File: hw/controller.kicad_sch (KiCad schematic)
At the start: 16 parts, among them J1 BNC, J201 1935776, SW201 SW_Push, U201 MCU_Nucleo_L432KC

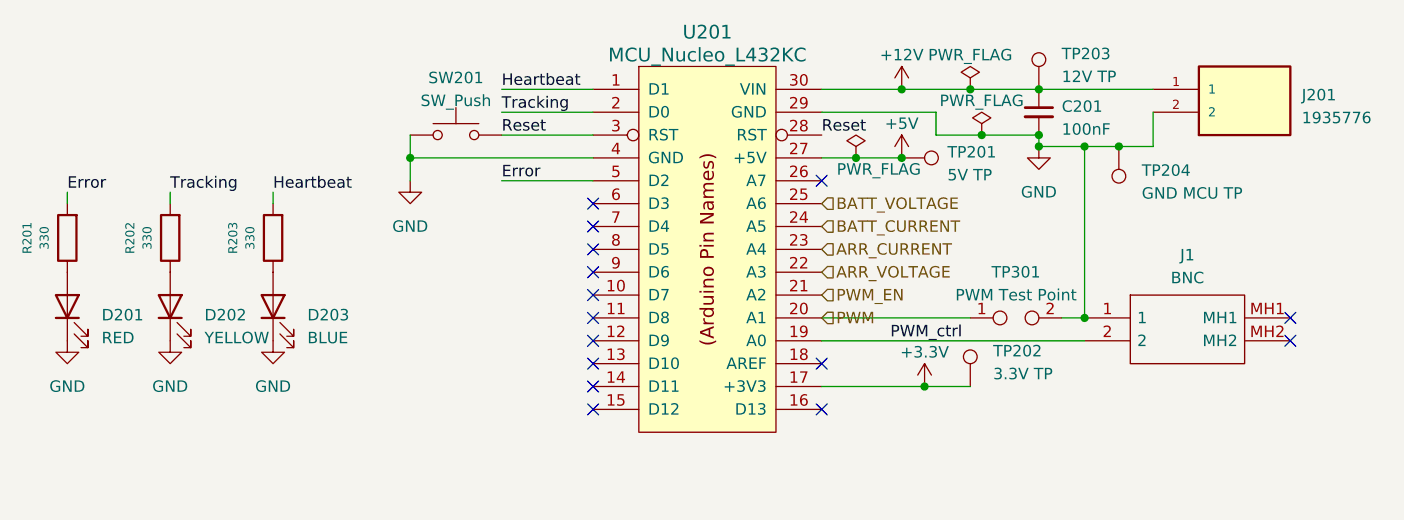
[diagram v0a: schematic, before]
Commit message: rebuild schematic, passes ERC, bom completed
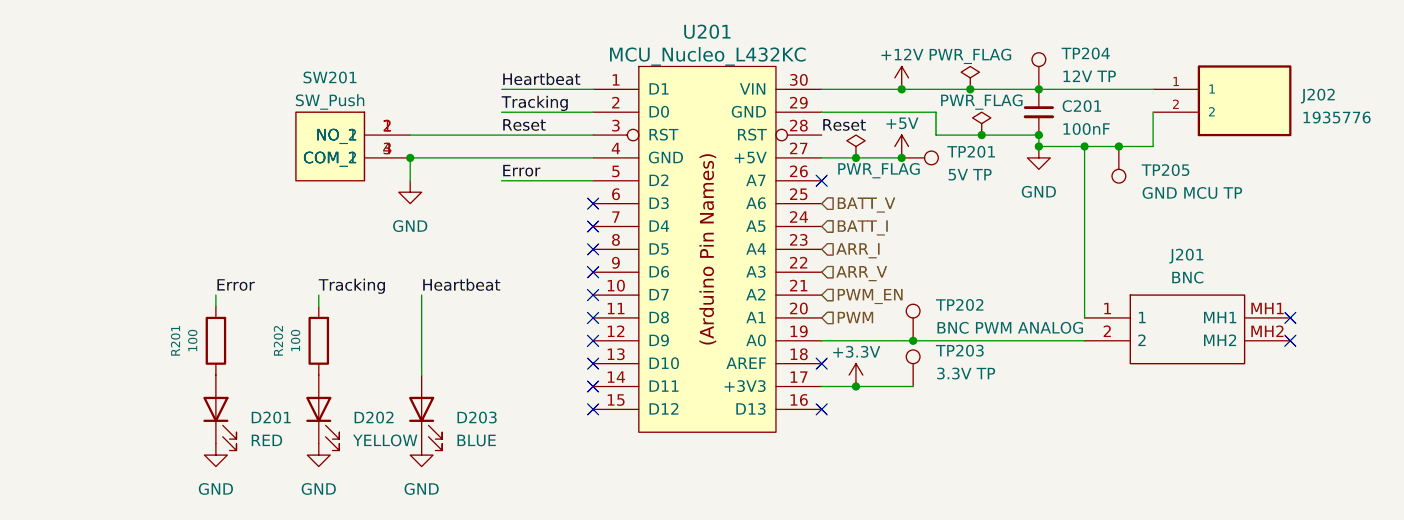
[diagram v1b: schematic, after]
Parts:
- removed R203: 330, Resistor_SMD:R_0805_2012Metric, symbol Device:R
- removed TP301: PWM Test Point, mppt:SignalTP, symbol Connector:TestPoint_2Pole
- added TP202: BNC PWM ANALOG, TestPoint:TestPoint_Keystone_5000-5004_Miniature, symbol Connector:TestPoint
- C201: Distributor (none) -> JLCPCB; In Stock? Y -> (none); JLC P/N (none) -> C307331; Manufacturer (none) -> Samsung Electro-Mechanics; Mfr PN CL21B104KCFNNNE -> (none); P/N (none) -> CL05B104KB54PNC; Projected Cost 0.008 -> (none)
- D201: footprint LED_SMD:LED_0805_2012Metric -> LED_SMD:LED_0402_1005Metric; Distributor (none) -> Mouser; In stock? Y -> (none); Manufacturer (none) -> Kingbright; Mfr PN NCD0805R1 -> (none); P/N (none) -> 604-APHHS1005SURCK; Projected Cost 0.0114 -> (none)
- D202: footprint LED_SMD:LED_0805_2012Metric -> LED_SMD:LED_0402_1005Metric; Distributor (none) -> Mouser; In Stock? Y -> (none); Manufacturer (none) -> Kingbright; Mfr PN SZYY0805YG -> (none); P/N (none) -> 604-APHHS1005SYCK; Projected Cost 0.0123 -> (none)
- D203: footprint LED_SMD:LED_0805_2012Metric -> LED_SMD:LED_0402_1005Metric; Distributor (none) -> Mouser; In Stock? Y -> (none); Manufacturer (none) -> Kingbright; Mfr PN SZYY0805B -> (none); P/N (none) -> 604-APHHS1005QBCD; Projected Cost 0.0129 -> (none)
- J201: renamed from J1; Distributor (none) -> Digikey; Manufacturer (none) -> Adam Tech; Manufacturer_Part_Number RF1-01A-D-00-75-M -> (none); P/N (none) -> 2057-RF1-01A-D-00-75-M-ND
- J202: renamed from J201; footprint 1935776 -> mppt:1935776; DESCRIPTION Fixed Terminal Blocks PT 2.5/ 2-5.0-H g -> (none); Distributor (none) -> Mouser; HEIGHT 13.5mm -> (none); In Stock? Y -> (none); MANUFACTURER_NAME Phoenix Contact -> (none); MANUFACTURER_PART_NUMBER 1935776 -> (none); MOUSER_PART_NUMBER 651-1935776 -> (none); MOUSER_PRICE-STOCK https://www.mouser.co.uk/ProductDetail/Phoenix-Contact/1935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 -> (none); Manufacturer (none) -> Phoenix Contact; P/N (none) -> 651-1935776; Projected Cost 0.59 -> (none)
- R201, R202: value 330 -> 100; footprint Resistor_SMD:R_0805_2012Metric -> Resistor_SMD:R_0402_1005Metric; In Stock? Y -> (none); JLC P/N (none) -> C25076; JLCPCB BOM 1 -> (none); LCSC Part C17630 -> (none); Manufacturer Part Number 0805W8F3300T5E -> (none); Mouser Part N/A -> (none); P/N (none) -> 0402WGF1000TCE; Projected Cost 0.0024 -> (none); Purchase Page N/A -> (none)
- SW201: footprint Button_Switch_THT:SW_PUSH_6mm -> mppt:TS046643BK100SMT; symbol Switch:SW_Push -> TS04-66-43-BK-100-SMT:TS04-66-43-BK-100-SMT; Distributor (none) -> Mouser; Manufacturer (none) -> CUI Devices; P/N (none) -> 179-TS046643BK100SMT
- TP201: Color (none) -> Red; Distributor (none) -> Mouser; Manufacturer (none) -> Keystone Electronics; P/N (none) -> 534-5000
- TP203: renamed from TP202; Color (none) -> Red; Distributor (none) -> Mouser; Manufacturer (none) -> Keystone Electronics; P/N (none) -> 534-5000
- TP204: renamed from TP203; Color (none) -> Red; Distributor (none) -> Mouser; Manufacturer (none) -> Keystone Electronics; P/N (none) -> 534-5000
- TP205: renamed from TP204; Color (none) -> Black; Distributor (none) -> Mouser; Manufacturer (none) -> Keystone Electronics; P/N (none) -> 534-5001
- U201: Distributor (none) -> Mouser; In Stock? N/A -> (none); Manufacturer (none) -> STMicroelectronics; P/N (none) -> 511-NUCLEO-L432KC
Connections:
- net GND: now also SW201.3 (COM_1), SW201.4 (COM_2); no longer SW201.1
- net Heartbeat: now also D203.2 (A)
- net Reset: now also SW201.1 (NO_1)
- net ARR_CURRENT renamed ARR_I
- net ARR_VOLTAGE renamed ARR_V
- net BATT_CURRENT renamed BATT_I
- net BATT_VOLTAGE renamed BATT_V
- net PWM_ctrl: no longer names the net of J201.2, U201.19 (A0)
- net PWM_ctrl: now also TP202.1
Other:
- moved on the sheet: D201, D202, D203, R201, R202, TP203

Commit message: savestate layout
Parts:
- removed J201: BNC, mppt:CONBNC002, symbol CONBNC002:CONBNC002
- removed TP202: BNC PWM ANALOG, TestPoint:TestPoint_Keystone_5000-5004_Miniature, symbol Connector:TestPoint
- added J202: BNC, mppt:CONBNC002, symbol CONBNC002:CONBNC002
- added TP204: TestPoint_2Pole, mppt:SignalTP, symbol Connector:TestPoint_2Pole
- renumbered J202 to J201, TP203 to TP202, TP204 to TP203
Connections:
- net GND: now also J202.2, J202.MH1, J202.MH2, TP204.2
- net at U201.19 (A0): now also J202.1, TP204.1
- no-connect marks 15 -> 13

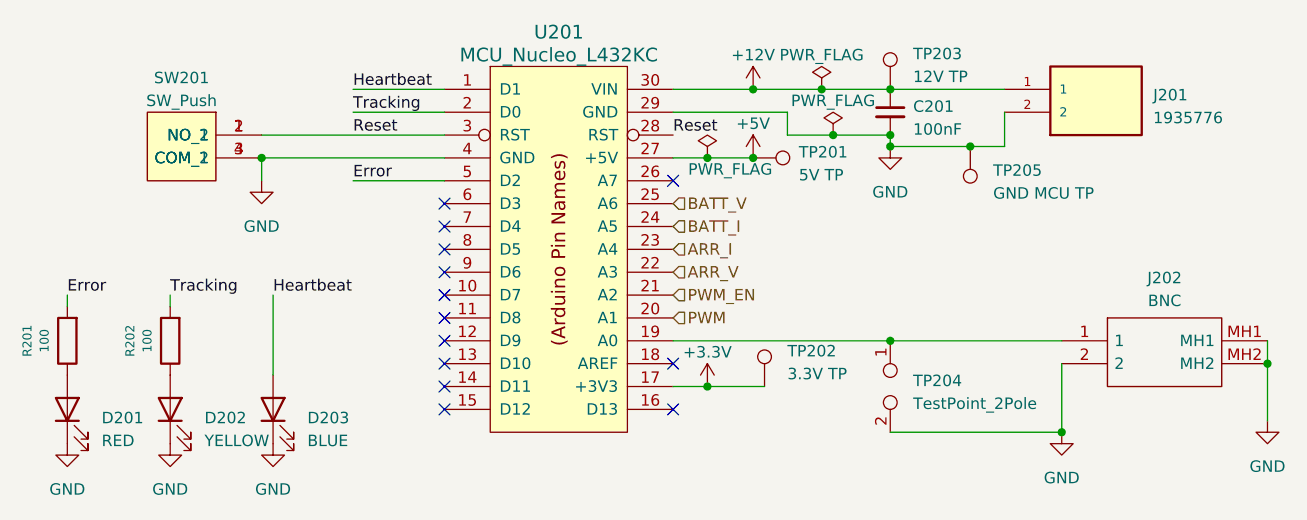
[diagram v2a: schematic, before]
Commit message: production files for v0.1.0. Change cap power calc to be based off i_rms of i_pkpk, not i_pk + r_l_a
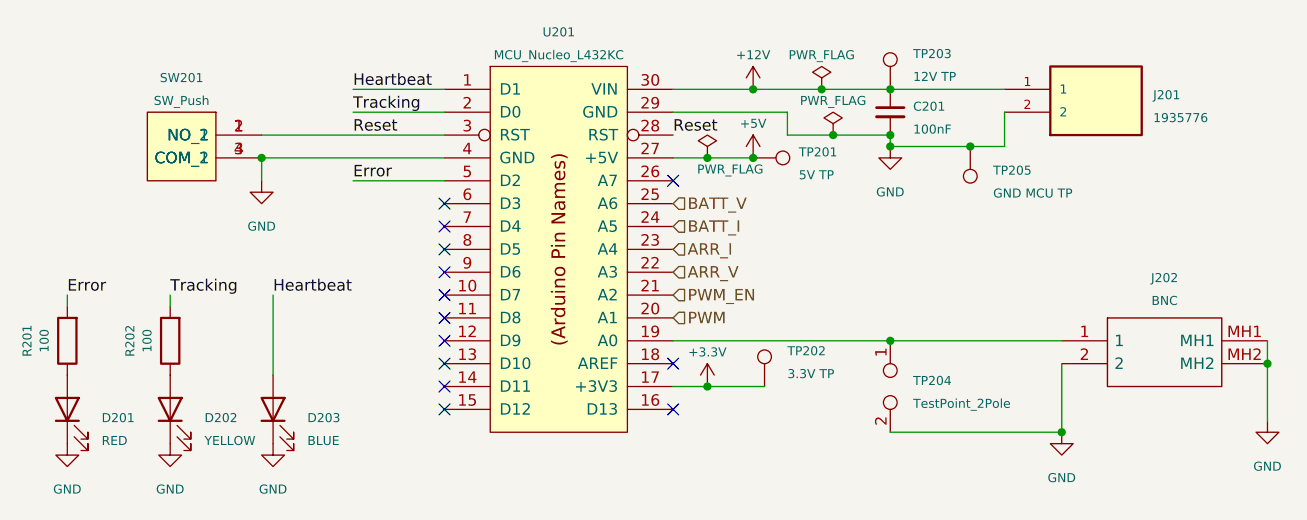
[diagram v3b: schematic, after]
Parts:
- C201: LCSC Part # (none) -> C307331
- R201, R202: LCSC Part # (none) -> C25076

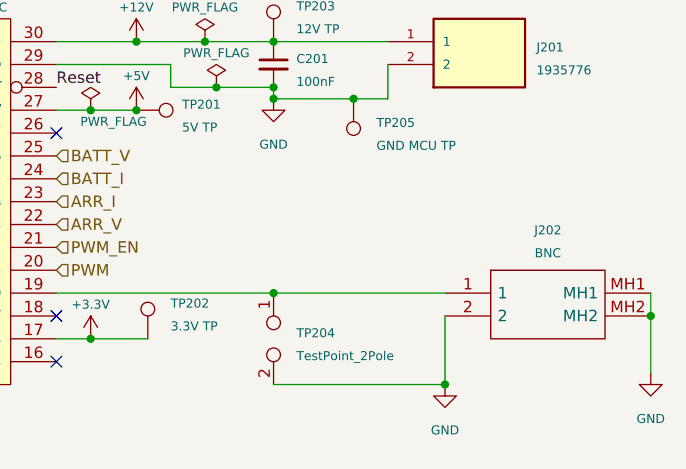
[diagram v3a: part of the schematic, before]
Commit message: fixed gate driver circuit, filleted filled zones, ensured DRC conformity regarding clearances
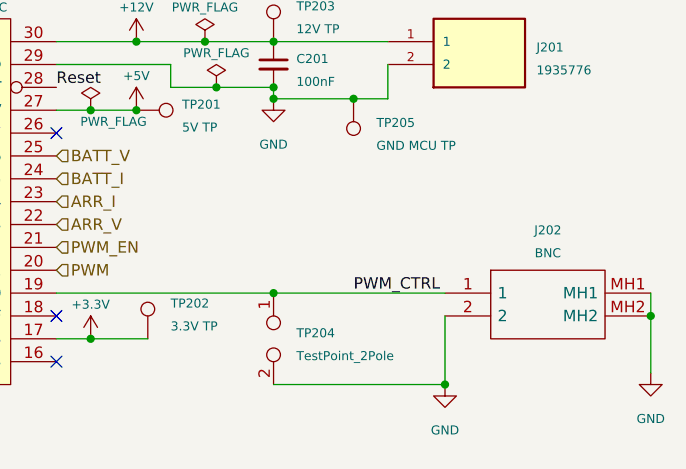
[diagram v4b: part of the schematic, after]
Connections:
- net PWM_CTRL: now reaches J202.1, TP204.1, U201.19 (A0)
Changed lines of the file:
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@@
+    (effects (font (size 1.27 1.27)) (justify left bottom))
+  )
+  (label "PWM_CTRL" (at 199.39 100.33 0) (fields_autoplaced)
     (effects (font (size 1.27 1.27)) (justify left bottom))
   )

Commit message: fixes for v0.1.1rc
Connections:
- net Error: now also U201.6 (D3); no longer U201.5 (D2)
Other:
- note added: "I2C1_SCL"
- note added: "I2C1_SDA"
- note added: "USB_DM|CAN1_RD"
- note added: "USB_DP|CAN1_TD"
- company: (none) -> UT LHR Solar
- title: MPPT -> Sunscatter MPPT
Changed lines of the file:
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@@
   (paper "A4")
   (title_block
-    (title "MPPT")
-    (date "2023-01-30")
-    (rev "v0.0.0")
-    (comment 1 "Nishant Gupta")
+    (title "Sunscatter MPPT")
+    (date "2023-03-26")
+    (rev "v0.1.1")
+    (company "UT LHR Solar")
+    (comment 1 "Matthew Yu")
     (comment 2 "Jacob Pustilnik")
   )
@@
   (no_connect (at 166.37 82.55))
   (no_connect (at 140.97 107.95))
-  (no_connect (at 140.97 85.09))
   (no_connect (at 140.97 87.63))
+  (no_connect (at 140.97 82.55))
   (no_connect (at 166.37 102.87))
   (wire (pts (xy 110.49 95.25) (xy 110.49 96.52))
@@
   )
   (wire (pts (xy 166.37 100.33) (xy 190.5 100.33))
+    (stroke (width 0) (type default))
+  )
+  (wire (pts (xy 130.81 85.09) (xy 140.97 85.09))
     (stroke (width 0) (type default))
   )
@@
   )
   (wire (pts (xy 170.18 105.41) (xy 176.53 105.41))
-    (stroke (width 0) (type default))
-  )
-  (wire (pts (xy 130.81 82.55) (xy 140.97 82.55))
     (stroke (width 0) (type default))
   )
@@
     (stroke (width 0) (type default))
   )
+  (text_box "D2 and D10 are reserved for USB and CAN communication.\nD4 and D5 are reserved for I2C communication to irradiance, temperature sensors."
+    (at 16.51 16.51 0) (size 62.23 7.62)
+    (stroke (width 0) (type default))
+    (fill (type none))
+    (effects (font (size 1.27 1.27)) (justify left top))
+  )
+  (text "USB_DP|CAN1_TD" (at 138.43 82.55 0)
+    (effects (font (size 1 1)) (justify right bottom))
+  )
+  (text "I2C1_SDA" (at 138.43 87.63 0)
+    (effects (font (size 1 1)) (justify right bottom))
+  )
+  (text "I2C1_SCL" (at 138.43 90.17 0)
+    (effects (font (size 1 1)) (justify right bottom))
+  )
+  (text "USB_DM|CAN1_RD" (at 138.43 102.87 0)
+    (effects (font (size 1 1)) (justify right bottom))
+  )
   (label "Heartbeat" (at 130.81 72.39 0) (fields_autoplaced)
     (effects (font (size 1.27 1.27)) (justify left bottom))
@@
     (effects (font (size 1.27 1.27)) (justify left bottom))
   )
-  (label "Error" (at 130.81 82.55 0) (fields_autoplaced)
+  (label "Error" (at 130.81 85.09 0) (fields_autoplaced)
     (effects (font (size 1.27 1.27)) (justify left bottom))
   )

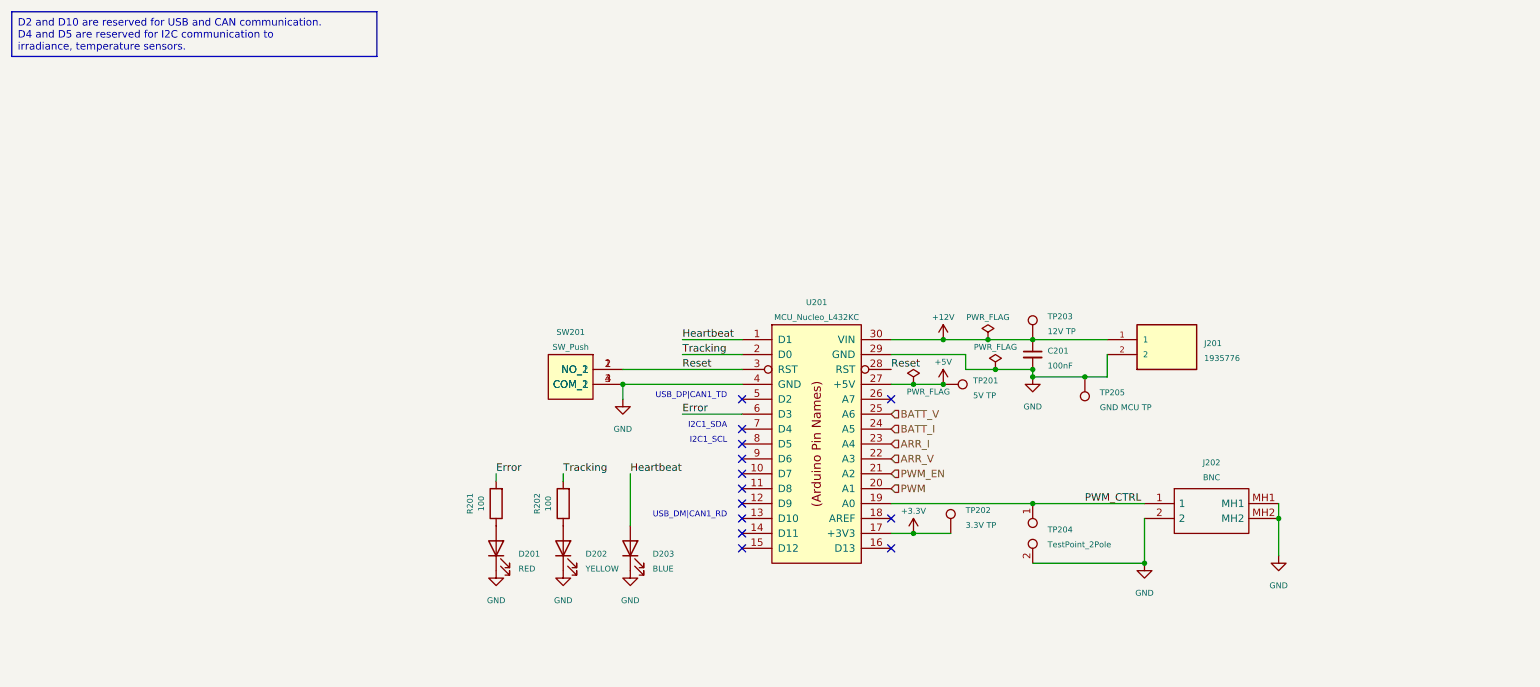
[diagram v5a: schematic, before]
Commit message: updated instructions for v0.2.0 - v0.5.0 development candidates.
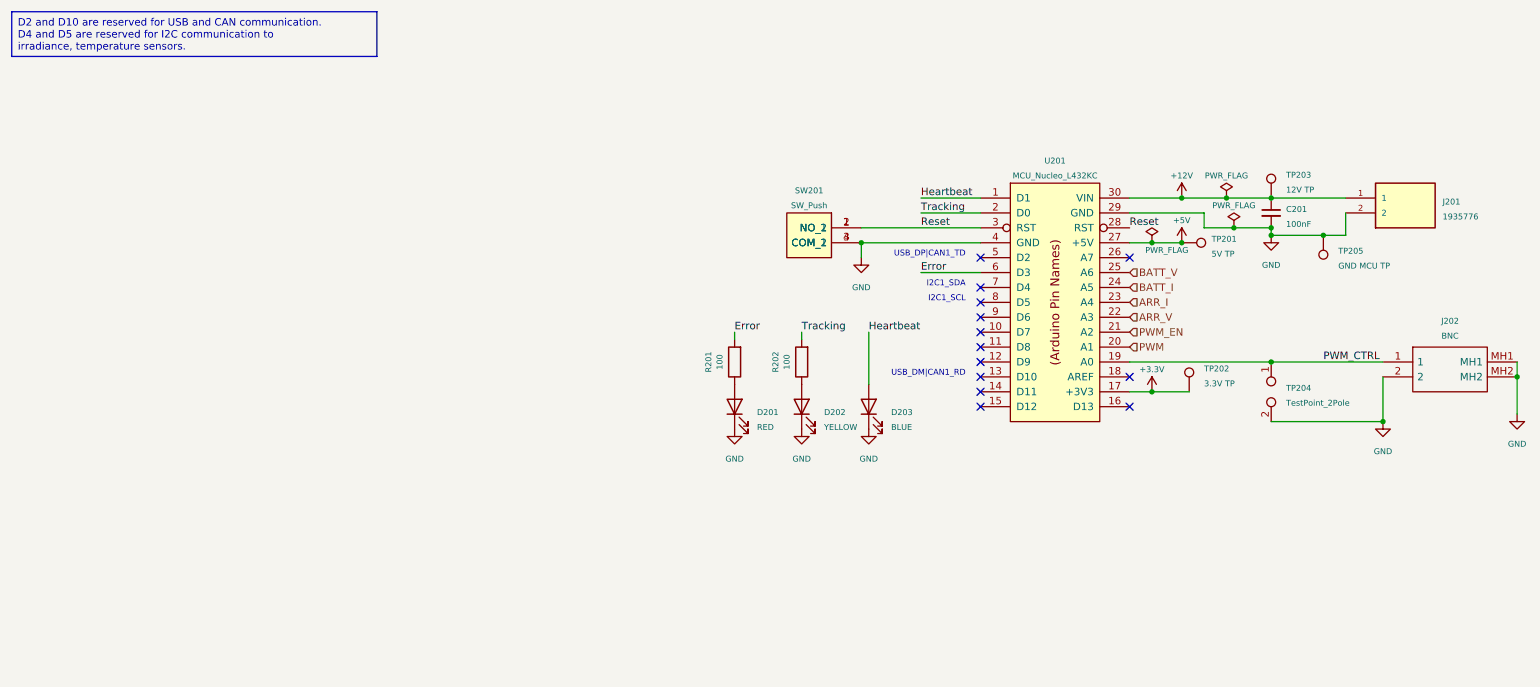
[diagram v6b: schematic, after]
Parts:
- C201: Cost (none) -> 0.0068; JLC P/N C307331 -> (none)
- D201: Cost (none) -> 0.43
- D202: Cost (none) -> 0.34
- D203: Cost (none) -> 0.37
- J201: Cost (none) -> 0.59
- J202: Cost (none) -> 2.39
- R201, R202: Cost (none) -> 0.0005; JLC P/N C25076 -> (none)
- SW201: Cost (none) -> 0.19
- TP201, TP202, TP203: Cost (none) -> 0.36
- TP205: Cost (none) -> 0.31
- U201: Cost (none) -> 10.99
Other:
- moved on the sheet: C201, D201, D202, D203, J201, J202, R201, R202, SW201, TP201, TP202, TP203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

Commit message: hw changes
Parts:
- J201: footprint mppt:1935776 -> footprints:1935776
- J202: footprint mppt:CONBNC002 -> footprints:CONBNC002
- SW201: footprint mppt:TS046643BK100SMT -> footprints:TS046643BK100SMT
- TP204: footprint mppt:SignalTP -> footprints:SignalTP
- U201: footprint mppt:MODULE_NUCLEO-L432KC -> footprints:MODULE_NUCLEO-L432KC
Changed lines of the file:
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@@
       (effects (font (size 1 1)))
     )
-    (property "Footprint" "mppt:MODULE_NUCLEO-L432KC" (at 194.31 73.66 0)
+    (property "Footprint" "footprints:MODULE_NUCLEO-L432KC" (at 194.31 73.66 0)
       (effects (font (size 1.524 1.524)) hide)
     )
@@
       (effects (font (size 1 1)))
     )
-    (property "Footprint" "mppt:CONBNC002" (at 269.24 73.66 0)
+    (property "Footprint" "footprints:CONBNC002" (at 269.24 73.66 0)
       (effects (font (size 1.27 1.27)) (justify left) hide)
     )
@@
       (effects (font (size 1 1)))
     )
-    (property "Footprint" "mppt:TS046643BK100SMT" (at 134.62 50.8 0)
+    (property "Footprint" "footprints:TS046643BK100SMT" (at 134.62 50.8 0)
       (effects (font (size 1.27 1.27)) (justify left) hide)
     )
@@
       (effects (font (size 1 1)) (justify left))
     )
-    (property "Footprint" "mppt:1935776" (at 243.84 48.26 0)
+    (property "Footprint" "footprints:1935776" (at 243.84 48.26 0)
       (effects (font (size 1.27 1.27)) (justify bottom) hide)
     )
@@
       (effects (font (size 1 1)) (justify left))
     )
-    (property "Footprint" "mppt:SignalTP" (at 231.14 81.28 0)
-      (effects (font (size 1.27 1.27)) hide)
-    )
+    (property "Footprint" "footprints:SignalTP" (at 231.14 81.28 0)
+      (effects (font (size 1.27 1.27)) hide)
+    )
